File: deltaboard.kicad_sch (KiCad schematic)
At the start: 49 parts, among them J1 USB_C_Receptacle, J4 SM03B-SRSS-TB, SW1 SW_Push, SW2 SW_Push, U1 RP2350_80QFN, U2 NCP1117-3.3_SOT223, U3 W25Q128JVS, U4 DNF, Y1 ABM8-272-T3

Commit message: sajdashdjasdh
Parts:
- removed SW2: SW_Push, Button_Switch_SMD:SW_Push_1P1T_NO_Vertical_Wuerth_434133025816, symbol Switch:SW_Push
- added D1: D, symbol Device:D
- added JP1, JP2: Jumper_2_Open, symbol Jumper:Jumper_2_Open
- SW1: footprint Button_Switch_SMD:SW_Push_1P1T_NO_Vertical_Wuerth_434133025816 -> (none)
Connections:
- net GND: now also JP1.1 (A); no longer SW1.1
- net RUN: now also JP2.2 (B)
- net ~{USB_BOOT}: now also JP1.2 (B); no longer SW1.2
- net at R4.1: now also JP2.1 (A)
- new net: D1.2 (A), SW1.2
- new net COL0: SW1.1
- new net ROW0: D1.1 (K)
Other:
- note added: "BOOTSEL"
- note added: "RUN"

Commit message: add switches
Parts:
- removed SW1: SW_Push, symbol Switch:SW_Push
- added D10, D11, D12, D13, D14, D15, D16, D17, D18, D19, D2, D20, D21, D22, D23, D24, D25, D26, D27, D28, D29, D3, D30, D31, D32, D33, D34, D35, D36, D37, D38, D39, D4, D40, D41, D42, D43, D44, D45, D46, D47, D48, D49, D5, D50, D51, D52, D53, D54, D55, D56, D57, D58, D59, D6, D60, D61, D62, D63, D64, D65, D66, D67, D68, D69, D7, D70, D71, D72, D73, D74, D75, D76, D77, D78, D79, D8, D80, D81, D82, D83, D84, D9: D, Diode_SMD:D_0805_2012Metric_Pad1.15x1.40mm_HandSolder, symbol Device:D
- added K1: Esc, Button_Switch_Keyboard:SW_Cherry_MX_1.00u_PCB, symbol Switch:SW_Push
- added K10: F9, Button_Switch_Keyboard:SW_Cherry_MX_1.00u_PCB, symbol Switch:SW_Push
- added K11: F10, Button_Switch_Keyboard:SW_Cherry_MX_1.00u_PCB, symbol Switch:SW_Push
- added K12: F11, Button_Switch_Keyboard:SW_Cherry_MX_1.00u_PCB, symbol Switch:SW_Push
- added K13: ~~,`, Button_Switch_Keyboard:SW_Cherry_MX_1.00u_PCB, symbol Switch:SW_Push
- added K14: !,1, Button_Switch_Keyboard:SW_Cherry_MX_1.00u_PCB, symbol Switch:SW_Push
- added K15: @,2, Button_Switch_Keyboard:SW_Cherry_MX_1.00u_PCB, symbol Switch:SW_Push
- added K16: #,3, Button_Switch_Keyboard:SW_Cherry_MX_1.00u_PCB, symbol Switch:SW_Push
- added K17: $,4, Button_Switch_Keyboard:SW_Cherry_MX_1.00u_PCB, symbol Switch:SW_Push
- added K18: %,5, Button_Switch_Keyboard:SW_Cherry_MX_1.00u_PCB, symbol Switch:SW_Push
- added K19: ^,6, Button_Switch_Keyboard:SW_Cherry_MX_1.00u_PCB, symbol Switch:SW_Push
- added K2: F1, Button_Switch_Keyboard:SW_Cherry_MX_1.00u_PCB, symbol Switch:SW_Push
- added K20: &,7, Button_Switch_Keyboard:SW_Cherry_MX_1.00u_PCB, symbol Switch:SW_Push
- added K21: *,8, Button_Switch_Keyboard:SW_Cherry_MX_1.00u_PCB, symbol Switch:SW_Push
- added K22: (,9, Button_Switch_Keyboard:SW_Cherry_MX_1.00u_PCB, symbol Switch:SW_Push
- added K23: ),0, Button_Switch_Keyboard:SW_Cherry_MX_1.00u_PCB, symbol Switch:SW_Push
- added K24: _,-, Button_Switch_Keyboard:SW_Cherry_MX_1.00u_PCB, symbol Switch:SW_Push
- added K25: +,=, Button_Switch_Keyboard:SW_Cherry_MX_1.00u_PCB, symbol Switch:SW_Push
- added K26: Backspace, Button_Switch_Keyboard:SW_Cherry_MX_2.00u_PCB, symbol Switch:SW_Push
- added K27: F12, Button_Switch_Keyboard:SW_Cherry_MX_1.00u_PCB, symbol Switch:SW_Push
- added K28: Insert, Button_Switch_Keyboard:SW_Cherry_MX_1.00u_PCB, symbol Switch:SW_Push
- added K29: Home, Button_Switch_Keyboard:SW_Cherry_MX_1.00u_PCB, symbol Switch:SW_Push
- added K3: F2, Button_Switch_Keyboard:SW_Cherry_MX_1.00u_PCB, symbol Switch:SW_Push
- added K30: Tab, Button_Switch_Keyboard:SW_Cherry_MX_1.50u_PCB, symbol Switch:SW_Push
- added K31: Q, Button_Switch_Keyboard:SW_Cherry_MX_1.00u_PCB, symbol Switch:SW_Push
- added K32: W, Button_Switch_Keyboard:SW_Cherry_MX_1.00u_PCB, symbol Switch:SW_Push
- added K33: E, Button_Switch_Keyboard:SW_Cherry_MX_1.00u_PCB, symbol Switch:SW_Push
- added K34: R, Button_Switch_Keyboard:SW_Cherry_MX_1.00u_PCB, symbol Switch:SW_Push
- added K35: T, Button_Switch_Keyboard:SW_Cherry_MX_1.00u_PCB, symbol Switch:SW_Push
- added K36: Y, Button_Switch_Keyboard:SW_Cherry_MX_1.00u_PCB, symbol Switch:SW_Push
- added K37: U, Button_Switch_Keyboard:SW_Cherry_MX_1.00u_PCB, symbol Switch:SW_Push
- added K38: I, Button_Switch_Keyboard:SW_Cherry_MX_1.00u_PCB, symbol Switch:SW_Push
- added K39: O, Button_Switch_Keyboard:SW_Cherry_MX_1.00u_PCB, symbol Switch:SW_Push
- added K4: F3, Button_Switch_Keyboard:SW_Cherry_MX_1.00u_PCB, symbol Switch:SW_Push
- added K40: P, Button_Switch_Keyboard:SW_Cherry_MX_1.00u_PCB, symbol Switch:SW_Push
- added K41: {,[, Button_Switch_Keyboard:SW_Cherry_MX_1.00u_PCB, symbol Switch:SW_Push
- added K42: },], Button_Switch_Keyboard:SW_Cherry_MX_1.00u_PCB, symbol Switch:SW_Push
- added K43: |,\, Button_Switch_Keyboard:SW_Cherry_MX_1.50u_PCB, symbol Switch:SW_Push
- added K44: Delete, Button_Switch_Keyboard:SW_Cherry_MX_1.00u_PCB, symbol Switch:SW_Push
- added K45: End, Button_Switch_Keyboard:SW_Cherry_MX_1.00u_PCB, symbol Switch:SW_Push
- added K46: PgUp, Button_Switch_Keyboard:SW_Cherry_MX_1.00u_PCB, symbol Switch:SW_Push
- added K47: Caps Lock, Button_Switch_Keyboard:SW_Cherry_MX_1.75u_PCB, symbol Switch:SW_Push
- added K48: A, Button_Switch_Keyboard:SW_Cherry_MX_1.00u_PCB, symbol Switch:SW_Push
- added K49: S, Button_Switch_Keyboard:SW_Cherry_MX_1.00u_PCB, symbol Switch:SW_Push
- added K5: F4, Button_Switch_Keyboard:SW_Cherry_MX_1.00u_PCB, symbol Switch:SW_Push
- added K50: D, Button_Switch_Keyboard:SW_Cherry_MX_1.00u_PCB, symbol Switch:SW_Push
- added K51: F, Button_Switch_Keyboard:SW_Cherry_MX_1.00u_PCB, symbol Switch:SW_Push
- added K52: G, Button_Switch_Keyboard:SW_Cherry_MX_1.00u_PCB, symbol Switch:SW_Push
- added K53: H, Button_Switch_Keyboard:SW_Cherry_MX_1.00u_PCB, symbol Switch:SW_Push
- added K54: J, Button_Switch_Keyboard:SW_Cherry_MX_1.00u_PCB, symbol Switch:SW_Push
- added K55: K, Button_Switch_Keyboard:SW_Cherry_MX_1.00u_PCB, symbol Switch:SW_Push
- added K56: L, Button_Switch_Keyboard:SW_Cherry_MX_1.00u_PCB, symbol Switch:SW_Push
- added K57: :,;, Button_Switch_Keyboard:SW_Cherry_MX_1.00u_PCB, symbol Switch:SW_Push
- added K58: ",', Button_Switch_Keyboard:SW_Cherry_MX_1.00u_PCB, symbol Switch:SW_Push
- added K59: Enter, Button_Switch_Keyboard:SW_Cherry_MX_2.25u_PCB, symbol Switch:SW_Push
- added K6: F5, Button_Switch_Keyboard:SW_Cherry_MX_1.00u_PCB, symbol Switch:SW_Push
- added K60: Shift, Button_Switch_Keyboard:SW_Cherry_MX_2.25u_PCB, symbol Switch:SW_Push
- added K61: Z, Button_Switch_Keyboard:SW_Cherry_MX_1.00u_PCB, symbol Switch:SW_Push
- added K62: X, Button_Switch_Keyboard:SW_Cherry_MX_1.00u_PCB, symbol Switch:SW_Push
- added K63: C, Button_Switch_Keyboard:SW_Cherry_MX_1.00u_PCB, symbol Switch:SW_Push
- added K64: V, Button_Switch_Keyboard:SW_Cherry_MX_1.00u_PCB, symbol Switch:SW_Push
- added K65: B, Button_Switch_Keyboard:SW_Cherry_MX_1.00u_PCB, symbol Switch:SW_Push
- added K66: N, Button_Switch_Keyboard:SW_Cherry_MX_1.00u_PCB, symbol Switch:SW_Push
- added K67: M, Button_Switch_Keyboard:SW_Cherry_MX_1.00u_PCB, symbol Switch:SW_Push
- added K68: <,,, Button_Switch_Keyboard:SW_Cherry_MX_1.00u_PCB, symbol Switch:SW_Push
- added K69: >,., Button_Switch_Keyboard:SW_Cherry_MX_1.00u_PCB, symbol Switch:SW_Push
- added K7: F6, Button_Switch_Keyboard:SW_Cherry_MX_1.00u_PCB, symbol Switch:SW_Push
- added K70: ?,/, Button_Switch_Keyboard:SW_Cherry_MX_1.00u_PCB, symbol Switch:SW_Push
- added K71: Shift, Button_Switch_Keyboard:SW_Cherry_MX_2.75u_PCB, symbol Switch:SW_Push
- added K72: ↑, Button_Switch_Keyboard:SW_Cherry_MX_1.00u_PCB, symbol Switch:SW_Push
- added K73, K80: Ctrl, Button_Switch_Keyboard:SW_Cherry_MX_1.25u_PCB, symbol Switch:SW_Push
- added K74, K78: Win, Button_Switch_Keyboard:SW_Cherry_MX_1.25u_PCB, symbol Switch:SW_Push
- added K75, K77: Alt, Button_Switch_Keyboard:SW_Cherry_MX_1.25u_PCB, symbol Switch:SW_Push
- added K76: Blank, Button_Switch_Keyboard:SW_Cherry_MX_6.25u_PCB, symbol Switch:SW_Push
- added K79: Menu, Button_Switch_Keyboard:SW_Cherry_MX_1.25u_PCB, symbol Switch:SW_Push
- added K8: F7, Button_Switch_Keyboard:SW_Cherry_MX_1.00u_PCB, symbol Switch:SW_Push
- added K81: ←, Button_Switch_Keyboard:SW_Cherry_MX_1.00u_PCB, symbol Switch:SW_Push
- added K82: ↓, Button_Switch_Keyboard:SW_Cherry_MX_1.00u_PCB, symbol Switch:SW_Push
- added K83: PgDn, Button_Switch_Keyboard:SW_Cherry_MX_1.00u_PCB, symbol Switch:SW_Push
- added K84: →, Button_Switch_Keyboard:SW_Cherry_MX_1.00u_PCB, symbol Switch:SW_Push
- added K9: F8, Button_Switch_Keyboard:SW_Cherry_MX_1.00u_PCB, symbol Switch:SW_Push
- D1: footprint (none) -> Diode_SMD:D_0805_2012Metric_Pad1.15x1.40mm_HandSolder
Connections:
- net at D1.2 (A): now also K1.2
- net ROW0 renamed Row_0
- net Row_0: now also D10.1 (K), D11.1 (K), D12.1 (K), D2.1 (K), D27.1 (K), D3.1 (K), D4.1 (K), D5.1 (K), D6.1 (K), D7.1 (K), D8.1 (K), D9.1 (K)
- new net: D80.2 (A), K80.2
- new net: D49.2 (A), K49.2
- new net: D15.2 (A), K15.2
- new net: D6.2 (A), K6.2
- new net: D16.2 (A), K16.2
- new net: D41.2 (A), K41.2
- new net: D19.2 (A), K19.2
- new net: D36.2 (A), K36.2
- new net: D51.2 (A), K51.2
- new net: D47.2 (A), K47.2
- new net: D31.2 (A), K31.2
- new net: D61.2 (A), K61.2
- new net: D17.2 (A), K17.2
- new net: D13.2 (A), K13.2
- new net: D38.2 (A), K38.2
- new net: D53.2 (A), K53.2
- new net: D11.2 (A), K11.2
- new net: D12.2 (A), K12.2
- new net: D48.2 (A), K48.2
- new net: D52.2 (A), K52.2
- new net: D62.2 (A), K62.2
- new net: D66.2 (A), K66.2
- new net: D56.2 (A), K56.2
- new net: D34.2 (A), K34.2
- new net: D24.2 (A), K24.2
- new net: D35.2 (A), K35.2
- new net: D65.2 (A), K65.2
- new net: D8.2 (A), K8.2
- new net: D2.2 (A), K2.2
- new net: D55.2 (A), K55.2
- new net: D40.2 (A), K40.2
- new net: D75.2 (A), K75.2
- new net: D67.2 (A), K67.2
- new net: D25.2 (A), K25.2
- new net: D69.2 (A), K69.2
- new net: D79.2 (A), K79.2
- new net: D76.2 (A), K76.2
- new net: D23.2 (A), K23.2
- new net: D64.2 (A), K64.2
- new net: D39.2 (A), K39.2
- new net: D44.2 (A), K44.2
- new net: D30.2 (A), K30.2
- new net: D83.2 (A), K83.2
- new net: D10.2 (A), K10.2
- new net: D82.2 (A), K82.2
- new net: D7.2 (A), K7.2
- new net: D28.2 (A), K28.2
- new net: D20.2 (A), K20.2
- new net: D77.2 (A), K77.2
- new net: D46.2 (A), K46.2
- new net: D74.2 (A), K74.2
- new net: D14.2 (A), K14.2
- new net: D45.2 (A), K45.2
- new net: D29.2 (A), K29.2
- new net: D70.2 (A), K70.2
- new net: D9.2 (A), K9.2
- new net: D37.2 (A), K37.2
- new net: D63.2 (A), K63.2
- new net: D81.2 (A), K81.2
- new net: D5.2 (A), K5.2
- new net: D84.2 (A), K84.2
- new net: D50.2 (A), K50.2
- new net: D32.2 (A), K32.2
- new net: D60.2 (A), K60.2
- new net: D71.2 (A), K71.2
- new net: D33.2 (A), K33.2
- new net: D57.2 (A), K57.2
- new net: D4.2 (A), K4.2
- new net: D21.2 (A), K21.2
- new net: D27.2 (A), K27.2
- new net: D42.2 (A), K42.2
- new net: D78.2 (A), K78.2
- new net: D68.2 (A), K68.2
- new net: D54.2 (A), K54.2
- new net: D18.2 (A), K18.2
- new net: D22.2 (A), K22.2
- new net: D59.2 (A), K59.2
- new net: D72.2 (A), K72.2
- new net: D58.2 (A), K58.2
- new net: D73.2 (A), K73.2
- new net: D3.2 (A), K3.2
- new net: D43.2 (A), K43.2
- new net: D26.2 (A), K26.2
- new net Col_0: K1.1, K13.1, K30.1, K47.1, K60.1, K73.1
- new net Col_1: K14.1, K2.1, K31.1, K48.1, K61.1, K74.1
- new net Col_10: K11.1, K23.1, K40.1, K57.1, K70.1, K84.1
- new net Col_11: K12.1, K24.1, K41.1, K58.1, K71.1
- new net Col_12: K25.1, K27.1, K42.1, K59.1, K72.1
- new net Col_13: K26.1, K43.1
- new net Col_14: K28.1, K44.1
- new net Col_15: K29.1, K45.1
- new net Col_16: K46.1, K83.1
- new net Col_2: K15.1, K3.1, K32.1, K49.1, K62.1, K75.1
- new net Col_3: K16.1, K33.1, K4.1, K50.1, K63.1, K76.1
- new net Col_4: K17.1, K34.1, K5.1, K51.1, K64.1, K77.1
- new net Col_5: K18.1, K35.1, K52.1, K6.1, K65.1, K78.1
- new net Col_6: K19.1, K36.1, K53.1, K66.1, K7.1, K79.1
- new net Col_7: K20.1, K37.1, K54.1, K67.1, K8.1, K80.1
- new net Col_8: K21.1, K38.1, K55.1, K68.1, K81.1, K9.1
- new net Col_9: K10.1, K22.1, K39.1, K56.1, K69.1, K82.1
- new net Row_1: D13.1 (K), D14.1 (K), D15.1 (K), D16.1 (K), D17.1 (K), D18.1 (K), D19.1 (K), D20.1 (K), D21.1 (K), D22.1 (K), D23.1 (K), D24.1 (K), D25.1 (K), D26.1 (K), D28.1 (K), D29.1 (K), D46.1 (K)
- new net Row_2: D30.1 (K), D31.1 (K), D32.1 (K), D33.1 (K), D34.1 (K), D35.1 (K), D36.1 (K), D37.1 (K), D38.1 (K), D39.1 (K), D40.1 (K), D41.1 (K), D42.1 (K), D43.1 (K), D44.1 (K), D45.1 (K), D83.1 (K)
- new net Row_3: D47.1 (K), D48.1 (K), D49.1 (K), D50.1 (K), D51.1 (K), D52.1 (K), D53.1 (K), D54.1 (K), D55.1 (K), D56.1 (K), D57.1 (K), D58.1 (K), D59.1 (K)
- new net Row_4: D60.1 (K), D61.1 (K), D62.1 (K), D63.1 (K), D64.1 (K), D65.1 (K), D66.1 (K), D67.1 (K), D68.1 (K), D69.1 (K), D70.1 (K), D71.1 (K), D72.1 (K)
- new net Row_5: D73.1 (K), D74.1 (K), D75.1 (K), D76.1 (K), D77.1 (K), D78.1 (K), D79.1 (K), D80.1 (K), D81.1 (K), D82.1 (K), D84.1 (K)
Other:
- moved on the sheet: C6, C7, JP2, R4

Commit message: rename some labels
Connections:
- net Col_0 renamed COL_0
- net Col_1 renamed COL_1
- net Col_10 renamed COL_10
- net Col_11 renamed COL_11
- net Col_12 renamed COL_12
- net Col_13 renamed COL_13
- net Col_14 renamed COL_14
- net Col_15 renamed COL_15
- net Col_16 renamed COL_16
- net Col_2 renamed COL_2
- net Col_3 renamed COL_3
- net Col_4 renamed COL_4
- net Col_5 renamed COL_5
- net Col_6 renamed COL_6
- net Col_7 renamed COL_7
- net Col_8 renamed COL_8
- net Col_9 renamed COL_9
- net Row_0 renamed ROW_0
- net Row_1 renamed ROW_1
- net Row_2 renamed ROW_2
- net Row_3 renamed ROW_3
- net Row_4 renamed ROW_4
- net Row_5 renamed ROW_5
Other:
- moved on the sheet: D1, D10, D11, D12, D13, D14, D15, D16, D17, D18, D19, D2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

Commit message: feat: add switches and leds
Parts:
- removed C11, C12, C13: 100n, Capacitor_SMD:C_0402_1005Metric, symbol Device:C
- removed C4: 15p, Capacitor_SMD:C_0402_1005Metric, symbol Device:C
- removed C9: 4.7u, Capacitor_SMD:C_0402_1005Metric, symbol Device:C
- removed J4: SM03B-SRSS-TB, Connector_JST:JST_SH_SM03B-SRSS-TB_1x03-1MP_P1.00mm_Horizontal, symbol Connector_Generic_MountingPin:Conn_01x03_MountingPin
- removed K32: W, Button_Switch_Keyboard:SW_Cherry_MX_1.00u_PCB, symbol Switch:SW_Push
- removed L1: 3.3u, RP2350_80QFN_minimal:L_pol_2016, symbol Device:L
- removed R10: 0, Resistor_SMD:R_0402_1005Metric, symbol Device:R
- removed R11, R13: DNF, Resistor_SMD:R_0402_1005Metric, symbol Device:R
- removed R12: 5.1k, symbol Device:R
- removed R2, R4: 1k, Resistor_SMD:R_0402_1005Metric, symbol Device:R
- removed R3: 33, Resistor_SMD:R_0402_1005Metric, symbol Device:R
- removed U1: RP2350_80QFN, RP2350_80QFN_minimal:RP2350-QFN-80-1EP_10x10_P0.4mm_EP3.4x3.4mm_ThermalVias, symbol MCU_RaspberryPi_RP2350:RP2350_80QFN
- removed U4: DNF, Package_SO:SOIC-8_5.23x5.23mm_P1.27mm, symbol Memory_Flash:W25Q128JVS
- added C16: 100n, Capacitor_SMD:C_0402_1005Metric, symbol Device:C
- added C18, C19, C20, C23, C24, C25: 2.2uF, symbol Device:C
- added C2: 15p, Capacitor_SMD:C_0402_1005Metric, symbol Device:C
- added D85, D86, D87: D, Diode_SMD:D_0805_2012Metric_Pad1.15x1.40mm_HandSolder, symbol Device:D
- added H5, H6, H7, H8: MountingHole, MountingHole:MountingHole_2.7mm_M2.5, symbol Mechanical:MountingHole
- added J2: Conn_01x04, symbol Connector_Generic:Conn_01x04
- added K85: ↓, Button_Switch_Keyboard:SW_Cherry_MX_1.00u_PCB, symbol Switch:SW_Push
- added K86: PgDn, Button_Switch_Keyboard:SW_Cherry_MX_1.00u_PCB, symbol Switch:SW_Push
- added K87: →, Button_Switch_Keyboard:SW_Cherry_MX_1.00u_PCB, symbol Switch:SW_Push
- added LED1, LED10, LED11, LED12, LED13, LED14, LED15, LED16, LED17, LED18, LED19, LED2, LED20, LED21, LED22, LED23, LED24, LED25, LED26, LED27, LED28, LED29, LED3, LED30, LED31, LED32, LED33, LED34, LED35, LED36, LED37, LED38, LED39, LED4, LED40, LED41, LED42, LED43, LED44, LED45, LED46, LED47, LED48, LED49, LED5, LED50, LED51, LED52, LED53, LED54, LED55, LED56, LED57, LED58, LED59, LED6, LED60, LED61, LED62, LED63, LED64, LED65, LED66, LED67, LED68, LED69, LED7, LED70, LED71, LED72, LED73, LED74, LED75, LED76, LED77, LED78, LED79, LED8, LED80, LED81, LED82, LED83, LED84, LED85, LED86, LED9: SK6812MINI-E, neopixel.petty:SK6812MINI-E, symbol neopixel:SK6812MINI
- added R1: 1k, Resistor_SMD:R_0402_1005Metric, symbol Device:R
- added R8: 5.1k, symbol Device:R
- added SW1: SW_SPST, symbol Switch:SW_SPST
- added SW11: RotaryEncoder_Switch, Components:encoder, symbol Device:RotaryEncoder_Switch
- added U3: RP2040, RP2040_minimal:RP2040-QFN-56, symbol MCU_RaspberryPi_RP2040:RP2040
- C10: value 4.7u -> 1u
- C21: value 100n -> 2.2uF; footprint Capacitor_SMD:C_0402_1005Metric -> (none)
- C22: value DNF -> 2.2uF; footprint Capacitor_SMD:C_0402_1005Metric -> (none)
- C6, C7: value 4.7u -> 100n; footprint RP2350_80QFN_minimal:C_0402_1005Metric_small_pads -> Capacitor_SMD:C_0402_1005Metric
- C8: value 100n -> 1u
- K13: value ~~,` -> F12
- K14: value !,1 -> Blank
- K15: value @,2 -> Blank
- K16: value #,3 -> ~~,`
- K17: value $,4 -> !,1
- K18: value %,5 -> @,2
- K19: value ^,6 -> #,3
- K20: value &,7 -> $,4
- K21: value *,8 -> %,5
- K22: value (,9 -> ^,6
- K23: value ),0 -> &,7
- K24: value _,- -> *,8
- K25: value +,= -> (,9
- K26: value Backspace -> ),0; footprint Button_Switch_Keyboard:SW_Cherry_MX_2.00u_PCB -> Button_Switch_Keyboard:SW_Cherry_MX_1.00u_PCB
- K27: value F12 -> _,-
- K28: value Insert -> +,=
- K29: value Home -> Backspace; footprint Button_Switch_Keyboard:SW_Cherry_MX_1.00u_PCB -> Button_Switch_Keyboard:SW_Cherry_MX_2.00u_PCB
- K30: value Tab -> Insert; footprint Button_Switch_Keyboard:SW_Cherry_MX_1.50u_PCB -> Button_Switch_Keyboard:SW_Cherry_MX_1.00u_PCB
- K31: value Q -> Home
- K33: value E -> Tab; footprint Button_Switch_Keyboard:SW_Cherry_MX_1.00u_PCB -> Button_Switch_Keyboard:SW_Cherry_MX_1.50u_PCB
- K34: value R -> Q
- K35: value T -> W
- K36: value Y -> E
- K37: value U -> R
- K38: value I -> T
- K39: value O -> Y
- K40: value P -> U
- K41: value {,[ -> I
- K42: value },] -> O
- K43: value |,\ -> P; footprint Button_Switch_Keyboard:SW_Cherry_MX_1.50u_PCB -> Button_Switch_Keyboard:SW_Cherry_MX_1.00u_PCB
- K44: value Delete -> {,[
- K45: value End -> },]
- K46: value PgUp -> |,\; footprint Button_Switch_Keyboard:SW_Cherry_MX_1.00u_PCB -> Button_Switch_Keyboard:SW_Cherry_MX_1.50u_PCB
- K47: value Caps Lock -> Delete; footprint Button_Switch_Keyboard:SW_Cherry_MX_1.75u_PCB -> Button_Switch_Keyboard:SW_Cherry_MX_1.00u_PCB
- K48: value A -> End
- K49: value S -> PgUp
- K50: value D -> Caps Lock; footprint Button_Switch_Keyboard:SW_Cherry_MX_1.00u_PCB -> Button_Switch_Keyboard:SW_Cherry_MX_1.75u_PCB
- K51: value F -> A
- K52: value G -> S
- K53: value H -> D
- K54: value J -> F
- K55: value K -> G
- K56: value L -> H
- K57: value :,; -> J
- K58: value ",' -> K
- K59: value Enter -> L; footprint Button_Switch_Keyboard:SW_Cherry_MX_2.25u_PCB -> Button_Switch_Keyboard:SW_Cherry_MX_1.00u_PCB
- K60: value Shift -> :,;; footprint Button_Switch_Keyboard:SW_Cherry_MX_2.25u_PCB -> Button_Switch_Keyboard:SW_Cherry_MX_1.00u_PCB
- K61: value Z -> ",'
- K62: value X -> Enter; footprint Button_Switch_Keyboard:SW_Cherry_MX_1.00u_PCB -> Button_Switch_Keyboard:SW_Cherry_MX_2.25u_PCB
- K63: value C -> Shift; footprint Button_Switch_Keyboard:SW_Cherry_MX_1.00u_PCB -> Button_Switch_Keyboard:SW_Cherry_MX_2.25u_PCB
- K64: value V -> Z
- K65: value B -> X
- K66: value N -> C
- K67: value M -> V
- K68: value <,, -> B
- K69: value >,. -> N
- K70: value ?,/ -> M
- K71: value Shift -> <,,; footprint Button_Switch_Keyboard:SW_Cherry_MX_2.75u_PCB -> Button_Switch_Keyboard:SW_Cherry_MX_1.00u_PCB
- K72: value ↑ -> >,.
- K73: value Ctrl -> ?,/; footprint Button_Switch_Keyboard:SW_Cherry_MX_1.25u_PCB -> Button_Switch_Keyboard:SW_Cherry_MX_1.00u_PCB
- K74: value Win -> Shift; footprint Button_Switch_Keyboard:SW_Cherry_MX_1.25u_PCB -> Button_Switch_Keyboard:SW_Cherry_MX_2.75u_PCB
- K75: value Alt -> ↑; footprint Button_Switch_Keyboard:SW_Cherry_MX_1.25u_PCB -> Button_Switch_Keyboard:SW_Cherry_MX_1.00u_PCB
- K76: value Blank -> Ctrl; footprint Button_Switch_Keyboard:SW_Cherry_MX_6.25u_PCB -> Button_Switch_Keyboard:SW_Cherry_MX_1.25u_PCB
- K77: value Alt -> Win
- K78: value Win -> Alt
- K79: value Menu -> Blank; footprint Button_Switch_Keyboard:SW_Cherry_MX_1.25u_PCB -> Button_Switch_Keyboard:SW_Cherry_MX_6.25u_PCB
- K80: value Ctrl -> Alt
- K81: value ← -> Win; footprint Button_Switch_Keyboard:SW_Cherry_MX_1.00u_PCB -> Button_Switch_Keyboard:SW_Cherry_MX_1.25u_PCB
- K82: value ↓ -> Menu; footprint Button_Switch_Keyboard:SW_Cherry_MX_1.00u_PCB -> Button_Switch_Keyboard:SW_Cherry_MX_1.25u_PCB
- K83: value PgDn -> Ctrl; footprint Button_Switch_Keyboard:SW_Cherry_MX_1.00u_PCB -> Button_Switch_Keyboard:SW_Cherry_MX_1.25u_PCB
- K84: value → -> ←
- R5: value 5.1k -> 1k; footprint (none) -> Resistor_SMD:R_0402_1005Metric
- R6: footprint Resistor_SMD:R_0402_1005Metric -> (none)
- R9: value DNF -> 5.1k; footprint Resistor_SMD:R_0402_1005Metric -> (none)
- renumbered C15 to C11, C16 to C12, C17 to C13, C18 to C14, C20 to C15, C19 to C17, C5 to C4, C2 to C5, C14 to C9, R1 to R2, R7 to R3, R8 to R4, U2 to U1, U3 to U2
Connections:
- net +1V1: now also C6.1, U3.23 (DVDD), U3.45 (VREG_VOUT), U3.50 (DVDD); no longer C10.1
- net +3V3: now also C10.1, C16.1, U3.1 (IOVDD), U3.10 (IOVDD), U3.22 (IOVDD), U3.33 (IOVDD), U3.42 (IOVDD), U3.43 (ADC_AVDD), U3.44 (VREG_IN), U3.48 (USB_VDD), U3.49 (IOVDD); no longer C21.1, C22.1, C6.1
- net COL_0: now also K16.1, K33.1, K50.1, K63.1, K76.1, U3.8 (GPIO6); no longer K13.1, K30.1, K47.1, K60.1, K73.1
- net COL_1: now also K17.1, K34.1, K51.1, K64.1, K77.1, U3.9 (GPIO7); no longer K14.1, K31.1, K48.1, K61.1, K74.1
- net COL_10: now also K26.1, K43.1, K60.1, K73.1, K87.1, U3.27 (GPIO16); no longer K23.1, K40.1, K57.1, K70.1, K84.1
- net COL_11: now also K27.1, K44.1, K61.1, K74.1, U3.28 (GPIO17); no longer K24.1, K41.1, K58.1, K71.1
- net COL_12: now also K13.1, K28.1, K45.1, K62.1, K75.1, U3.29 (GPIO18); no longer K25.1, K27.1, K42.1, K59.1, K72.1
- net COL_13: now also K14.1, K29.1, K46.1, U3.30 (GPIO19); no longer K26.1, K43.1
- net COL_14: now also K15.1, K30.1, K47.1, U3.31 (GPIO20); no longer K28.1, K44.1
- net COL_16: now also K49.1, K86.1, U3.34 (GPIO22); no longer K46.1, K83.1
- net COL_2: now also K18.1, K35.1, K52.1, K65.1, K78.1, U3.11 (GPIO8); no longer K15.1, K49.1, K62.1, K75.1
- net COL_3: now also K19.1, K36.1, K53.1, K66.1, K79.1, U3.12 (GPIO9); no longer K16.1, K33.1, K50.1, K63.1, K76.1
- net COL_4: now also K20.1, K37.1, K54.1, K67.1, K80.1, U3.13 (GPIO10); no longer K17.1, K34.1, K51.1, K64.1, K77.1
- net COL_5: now also K21.1, K38.1, K55.1, K68.1, K81.1, U3.14 (GPIO11); no longer K18.1, K35.1, K52.1, K65.1, K78.1
- net COL_6: now also K22.1, K39.1, K56.1, K69.1, K82.1, U3.15 (GPIO12); no longer K19.1, K36.1, K53.1, K66.1, K79.1
- net COL_7: now also K23.1, K40.1, K57.1, K70.1, K83.1, U3.16 (GPIO13); no longer K20.1, K37.1, K54.1, K67.1, K80.1
- net COL_8: now also K24.1, K41.1, K58.1, K71.1, K84.1, U3.17 (GPIO14); no longer K21.1, K38.1, K55.1, K68.1, K81.1
- net COL_9: now also K25.1, K42.1, K59.1, K72.1, K85.1, U3.18 (GPIO15); no longer K22.1, K39.1, K56.1, K69.1, K82.1
- net GND: now also JP2.1 (A), R9.2, C16.2, C18.2, C19.2, C2.2, C20.2, C23.2, C24.2, C25.2, J2.1 (Pin_1), LED1.2 (VSS), LED10.2 (VSS), LED11.2 (VSS), LED12.2 (VSS), LED13.2 (VSS), LED14.2 (VSS), LED15.2 (VSS), LED16.2 (VSS), LED17.2 (VSS), LED18.2 (VSS), LED19.2 (VSS), LED2.2 (VSS), LED20.2 (VSS), LED21.2 (VSS), LED22.2 (VSS), LED23.2 (VSS), LED24.2 (VSS), LED25.2 (VSS), LED26.2 (VSS), LED27.2 (VSS), LED28.2 (VSS), LED29.2 (VSS), LED3.2 (VSS), LED30.2 (VSS), LED31.2 (VSS), LED32.2 (VSS), LED33.2 (VSS), LED34.2 (VSS), LED35.2 (VSS)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; no longer R5.2
- net GPIO0: now also D1.1 (K), D10.1 (K), D11.1 (K), D12.1 (K), D13.1 (K), D14.1 (K), D15.1 (K), D2.1 (K), D3.1 (K), D32.1 (K), D4.1 (K), D5.1 (K), D6.1 (K), D7.1 (K), D8.1 (K), D9.1 (K), U3.2 (GPIO0); no longer R9.1
- net GPIO1: now also D16.1 (K), D17.1 (K), D18.1 (K), D19.1 (K), D20.1 (K), D21.1 (K), D22.1 (K), D23.1 (K), D24.1 (K), D25.1 (K), D26.1 (K), D27.1 (K), D28.1 (K), D29.1 (K), D30.1 (K), D31.1 (K), D49.1 (K), U3.3 (GPIO1)
- net GPIO2: now also D33.1 (K), D34.1 (K), D35.1 (K), D36.1 (K), D37.1 (K), D38.1 (K), D39.1 (K), D40.1 (K), D41.1 (K), D42.1 (K), D43.1 (K), D44.1 (K), D45.1 (K), D46.1 (K), D47.1 (K), D48.1 (K), D86.1 (K), U3.4 (GPIO2)
- net GPIO3: now also D50.1 (K), D51.1 (K), D52.1 (K), D53.1 (K), D54.1 (K), D55.1 (K), D56.1 (K), D57.1 (K), D58.1 (K), D59.1 (K), D60.1 (K), D61.1 (K), D62.1 (K), U3.5 (GPIO3)
- net GPIO4: now also D63.1 (K), D64.1 (K), D65.1 (K), D66.1 (K), D67.1 (K), D68.1 (K), D69.1 (K), D70.1 (K), D71.1 (K), D72.1 (K), D73.1 (K), D74.1 (K), D75.1 (K), U3.6 (GPIO4)
- net GPIO5: now also D76.1 (K), D77.1 (K), D78.1 (K), D79.1 (K), D80.1 (K), D81.1 (K), D82.1 (K), D83.1 (K), D84.1 (K), D85.1 (K), D87.1 (K), U3.7 (GPIO5)
- net QSPI_SCLK: now also U3.52 (QSPI_SCLK)
- net QSPI_SD0: now also U3.53 (QSPI_SD0)
- net QSPI_SD1: now also U3.55 (QSPI_SD1)
- net QSPI_SD2: now also U3.54 (QSPI_SD2)
- net QSPI_SD3: now also U3.51 (QSPI_SD3)
- net QSPI_SS: now also R2.2, U2.1 (~{CS}), R1.1, U3.56 (QSPI_SS); no longer R6.1
- net RUN: now also R6.2, U3.26 (RUN); no longer JP2.2 (B)
- net SWCLK: now also U3.24 (SWCLK)
- net SWD: now also U3.25 (SWD)
- net VBUS: now also SW1.2 (B); no longer J1.A4 (VBUS), J1.A9 (VBUS), J1.B4 (VBUS), J1.B9 (VBUS)
- net XIN: now also C2.1, U3.20 (XIN); no longer C3.1
- net XOUT: now also R5.1, U3.21 (XOUT)
- net ~{USB_BOOT}: now also R1.2; no longer R6.2
- net at Y1.3: now also C3.1, R5.2
- net at R3.2: now also U3.47 (USB_DP)
- net at R4.2: now also U3.46 (USB_DM)
- net at J1.B5 (CC2): now also R9.1
- net at J1.A5 (CC1): now also R8.1; no longer R5.1
- net ENC_SWA: now reaches D32.2 (A)
- net ENC_SWA: now also SW11.S2
- removed net COL_15: K29.1, K45.1
- removed net FLASH_SS: R2.2, R9.2, U2.1 (~{CS})
- removed net ROW_0: D1.1 (K), D10.1 (K), D11.1 (K), D12.1 (K), D2.1 (K), D27.1 (K), D3.1 (K), D4.1 (K), D5.1 (K), D6.1 (K), D7.1 (K), D8.1 (K), D9.1 (K)
- removed net ROW_1: D13.1 (K), D14.1 (K), D15.1 (K), D16.1 (K), D17.1 (K), D18.1 (K), D19.1 (K), D20.1 (K), D21.1 (K), D22.1 (K), D23.1 (K), D24.1 (K), D25.1 (K), D26.1 (K), D28.1 (K), D29.1 (K), D46.1 (K)
- removed net ROW_2: D30.1 (K), D31.1 (K), D32.1 (K), D33.1 (K), D34.1 (K), D35.1 (K), D36.1 (K), D37.1 (K), D38.1 (K), D39.1 (K), D40.1 (K), D41.1 (K), D42.1 (K), D43.1 (K), D44.1 (K), D45.1 (K), D83.1 (K)
- removed net ROW_3: D47.1 (K), D48.1 (K), D49.1 (K), D50.1 (K), D51.1 (K), D52.1 (K), D53.1 (K), D54.1 (K), D55.1 (K), D56.1 (K), D57.1 (K), D58.1 (K), D59.1 (K)
- removed net ROW_4: D60.1 (K), D61.1 (K), D62.1 (K), D63.1 (K), D64.1 (K), D65.1 (K), D66.1 (K), D67.1 (K), D68.1 (K), D69.1 (K), D70.1 (K), D71.1 (K), D72.1 (K)
- removed net ROW_5: D73.1 (K), D74.1 (K), D75.1 (K), D76.1 (K), D77.1 (K), D78.1 (K), D79.1 (K), D80.1 (K), D81.1 (K), D82.1 (K), D84.1 (K)
- new net: D86.2 (A), K86.2
- new net: LED61.1 (DOUT), LED62.3 (DIN)
- new net: LED60.1 (DOUT), LED61.3 (DIN)
- new net: JP2.2 (B), R6.1
- new net: LED26.1 (DOUT), LED27.3 (DIN)
- new net: LED25.1 (DOUT), LED26.3 (DIN)
- new net: LED28.1 (DOUT), LED29.3 (DIN)
- new net: LED27.1 (DOUT), LED28.3 (DIN)
- new net: LED65.1 (DOUT), LED66.3 (DIN)
- new net: LED64.1 (DOUT), LED65.3 (DIN)
- new net: LED13.1 (DOUT), LED14.3 (DIN)
- new net: LED12.1 (DOUT), LED13.3 (DIN)
- new net: LED68.1 (DOUT), LED69.3 (DIN)
- new net: LED67.1 (DOUT), LED68.3 (DIN)
- new net: LED24.1 (DOUT), LED25.3 (DIN)
- new net: LED48.1 (DOUT), LED49.3 (DIN)
- new net: LED47.1 (DOUT), LED48.3 (DIN)
- new net: LED78.1 (DOUT), LED79.3 (DIN)
- new net: LED77.1 (DOUT), LED78.3 (DIN)
- new net: LED58.1 (DOUT), LED59.3 (DIN)
- new net: LED57.1 (DOUT), LED58.3 (DIN)
- new net: LED29.1 (DOUT), LED30.3 (DIN)
- new net: LED10.1 (DOUT), LED11.3 (DIN)
- new net: LED10.3 (DIN), LED9.1 (DOUT)
- new net: LED59.1 (DOUT), LED60.3 (DIN)
- new net: LED8.1 (DOUT), LED9.3 (DIN)
- new net: LED6.1 (DOUT), LED7.3 (DIN)
- new net: LED5.1 (DOUT), LED6.3 (DIN)
- new net: D87.2 (A), K87.2
- new net: LED83.1 (DOUT), LED84.3 (DIN)
- new net: LED82.1 (DOUT), LED83.3 (DIN)
- new net: LED79.1 (DOUT), LED80.3 (DIN)
- new net: LED31.1 (DOUT), LED32.3 (DIN)
- new net: LED30.1 (DOUT), LED31.3 (DIN)
- new net: LED7.1 (DOUT), LED8.3 (DIN)
- new net: LED38.1 (DOUT), LED39.3 (DIN)
- new net: LED37.1 (DOUT), LED38.3 (DIN)
- new net: LED72.1 (DOUT), LED73.3 (DIN)
- new net: LED71.1 (DOUT), LED72.3 (DIN)
- new net: LED81.1 (DOUT), LED82.3 (DIN)
- new net: LED20.1 (DOUT), LED21.3 (DIN)
- new net: LED19.1 (DOUT), LED20.3 (DIN)
- new net: LED18.1 (DOUT), LED19.3 (DIN)
- new net: LED17.1 (DOUT), LED18.3 (DIN)
- new net: LED56.1 (DOUT), LED57.3 (DIN)
- new net: LED55.1 (DOUT), LED56.3 (DIN)
- new net: LED85.1 (DOUT), LED86.3 (DIN)
- new net: LED53.1 (DOUT), LED54.3 (DIN)
- new net: LED52.1 (DOUT), LED53.3 (DIN)
- new net: LED51.1 (DOUT), LED52.3 (DIN)
- new net: LED50.1 (DOUT), LED51.3 (DIN)
- new net: LED16.1 (DOUT), LED17.3 (DIN)
- new net: D85.2 (A), K85.2
- new net: LED69.1 (DOUT), LED70.3 (DIN)
- new net: LED21.1 (DOUT), LED22.3 (DIN)
- new net: LED80.1 (DOUT), LED81.3 (DIN)
- new net: LED54.1 (DOUT), LED55.3 (DIN)
- new net: LED23.1 (DOUT), LED24.3 (DIN)
- new net: LED76.1 (DOUT), LED77.3 (DIN)
- new net: LED36.1 (DOUT), LED37.3 (DIN)
- new net: LED35.1 (DOUT), LED36.3 (DIN)
- new net: LED73.1 (DOUT), LED74.3 (DIN)
- new net: LED63.1 (DOUT), LED64.3 (DIN)
- new net: LED33.1 (DOUT), LED34.3 (DIN)
- new net: LED74.1 (DOUT), LED75.3 (DIN)
- new net: J1.A4 (VBUS), J1.A9 (VBUS), J1.B4 (VBUS), J1.B9 (VBUS), SW1.1 (A)
- new net: LED2.1 (DOUT), LED3.3 (DIN)
- new net: LED1.1 (DOUT), LED2.3 (DIN)
- new net: LED3.1 (DOUT), LED4.3 (DIN)
- new net: LED22.1 (DOUT), LED23.3 (DIN)
- new net: LED4.1 (DOUT), LED5.3 (DIN)
- new net: LED45.1 (DOUT), LED46.3 (DIN)
- new net: LED44.1 (DOUT), LED45.3 (DIN)
- new net: LED42.1 (DOUT), LED43.3 (DIN)
- new net: LED41.1 (DOUT), LED42.3 (DIN)
- new net: LED40.1 (DOUT), LED41.3 (DIN)
- new net: LED39.1 (DOUT), LED40.3 (DIN)
- new net: LED46.1 (DOUT), LED47.3 (DIN)
- new net: LED11.1 (DOUT), LED12.3 (DIN)
- new net: LED34.1 (DOUT), LED35.3 (DIN)
- new net: LED70.1 (DOUT), LED71.3 (DIN)
- new net: LED14.1 (DOUT), LED15.3 (DIN)
- new net: LED43.1 (DOUT), LED44.3 (DIN)
- new net: LED84.1 (DOUT), LED85.3 (DIN)
- new net: LED66.1 (DOUT), LED67.3 (DIN)
- new net ENC_1_A: SW11.A, U3.39 (GPIO27_ADC1)
- new net ENC_1_B: SW11.B, U3.38 (GPIO26_ADC0)
- new net ENC_SWB: K31.1, K48.1, SW11.S1, U3.32 (GPIO21)
- new net GPIO28_ADC2: U3.40 (GPIO28_ADC2)
- new net GPIO29_ADC3: U3.41 (GPIO29_ADC3)
- new net I2C_SCL: J2.3 (Pin_3), U3.37 (GPIO25)
- new net I2C_SDA: J2.4 (Pin_4), U3.36 (GPIO24)
- new net LED: LED1.3 (DIN), U3.35 (GPIO23)
- new net LED_OUT_0: LED15.1 (DOUT), LED16.3 (DIN)
- new net LED_OUT_1: LED32.1 (DOUT), LED33.3 (DIN)
- new net LED_OUT_2: LED49.1 (DOUT), LED50.3 (DIN)
- new net LED_OUT_3: LED62.1 (DOUT), LED63.3 (DIN)
- new net LED_OUT_4: LED75.1 (DOUT), LED76.3 (DIN)
- new net VCC: C18.1, C19.1, C20.1, C21.1, C22.1, C23.1, C24.1, C25.1, J2.2 (Pin_2), LED1.4 (VDD), LED10.4 (VDD), LED11.4 (VDD), LED12.4 (VDD), LED13.4 (VDD), LED14.4 (VDD), LED15.4 (VDD), LED16.4 (VDD), LED17.4 (VDD), LED18.4 (VDD), LED19.4 (VDD), LED2.4 (VDD), LED20.4 (VDD), LED21.4 (VDD), LED22.4 (VDD), LED23.4 (VDD), LED24.4 (VDD), LED25.4 (VDD), LED26.4 (VDD), LED27.4 (VDD), LED28.4 (VDD), LED29.4 (VDD), LED3.4 (VDD), LED30.4 (VDD), LED31.4 (VDD), LED32.4 (VDD), LED33.4 (VDD), LED34.4 (VDD), LED35.4 (VDD), LED36.4 (VDD), LED37.4 (VDD)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
- no-connect marks 0 -> 2
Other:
- note added: "Crystal"
- note added: "Flash"
- note added: "LEDs"
- note added: "MCU"
- note added: "Make sure C10 is close to pin 44 of RP2040"
- note added: "Make sure C8 is close to pin 45 of RP2040"
- note added: "Make sure R3 and R4 are close to RP2040"
- note added: "OLED"
- note added: "Pin Mappings"
- note added: "Switches"
- note removed: "12MHz Clock (Crystal)"
- note removed: "BOOTSEL"
- note removed: "JST Debug Connector"
- note removed: "Make sure R7 and R8 are close to RP2350"
- note removed: "Optional Secondary flash or PSRAM (U4), using the second chip select (XIP_SS_N[1]) on GPIO0. N.B. Pull-up R13 will be required as GPIOs default to pull-downs at power-up."
- note removed: "Primary Flash"
- note removed: "RUN"
- note removed: "Secondary Flash/PSRAM"
- moved on the sheet: C1, C11, C12, C13, C14, C15, C17, C4, C5, C9, H1, H2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

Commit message: update footprints
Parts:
- C18, C19, C20, C21, C22, C23, C24, C25: footprint (none) -> Capacitor_SMD:C_0603_1608Metric
- D1, D10, D11, D12, D13, D14, D15, D16, D17, D18, D19, D2, D20, D21, D22, D23, D24, D25, D26, D27, D28, D29, D3, D30, D31, D32, D33, D34, D35, D36, D37, D38, D39, D4, D40, D41, D42, D43, D44, D45, D46, D47, D48, D49, D5, D50, D51, D52, D53, D54, D55, D56, D57, D58, D59, D6, D60, D61, D62, D63, D64, D65, D66, D67, D68, D69, D7, D70, D71, D72, D73, D74, D75, D76, D77, D78, D79, D8, D80, D81, D82, D83, D84, D85, D86, D87, D9: footprint Diode_SMD:D_0805_2012Metric_Pad1.15x1.40mm_HandSolder -> Diode_SMD:D_SOD-123

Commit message: feat: place most leds
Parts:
- J1: footprint (none) -> Components:USB-C_SMD-TYPE-C-31-M-12
- J2: footprint (none) -> Components:SSD1306-0.91-OLED-4pin-128x32
- JP1, JP2: footprint (none) -> Jumper:SolderJumper-2_P1.3mm_Open_TrianglePad1.0x1.5mm
- R6, R8, R9: footprint (none) -> Resistor_SMD:R_0402_1005Metric
- U2: footprint Package_SO:SOIC-8_5.23x5.23mm_P1.27mm -> Components:SOIC-8_5.23x5.23mm_P1.27mm
- U3: footprint RP2040_minimal:RP2040-QFN-56 -> Components:RP2040-QFN-56
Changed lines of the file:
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@@
 			)
 		)
-		(property "Footprint" "RP2040_minimal:RP2040-QFN-56"
+		(property "Footprint" "Components:RP2040-QFN-56"
 			(at 462.28 260.35 0)
 			(effects
@@
 			)
 		)
-		(property "Footprint" "Package_SO:SOIC-8_5.23x5.23mm_P1.27mm"
+		(property "Footprint" "Components:SOIC-8_5.23x5.23mm_P1.27mm"
 			(at 472.44 121.92 0)
 			(effects
@@
 			)
 		)
-		(property "Footprint" ""
+		(property "Footprint" "Resistor_SMD:R_0402_1005Metric"
 			(at 431.8 282.448 90)
 			(effects
@@
 		(on_board yes)
 		(dnp no)
-		(fields_autoplaced yes)
 		(property "Reference" "LED16"
 			(at 36.83 198.12 0)
@@
 			)
 		)
-		(property "Footprint" ""
+		(property "Footprint" "Components:USB-C_SMD-TYPE-C-31-M-12"
 			(at 510.54 88.9 0)
 			(effects
@@
 			)
 		)
-		(property "Footprint" ""
+		(property "Footprint" "Jumper:SolderJumper-2_P1.3mm_Open_TrianglePad1.0x1.5mm"
 			(at 422.91 285.75 0)
 			(effects
@@
 			)
 		)
-		(property "Footprint" ""
+		(property "Footprint" "Jumper:SolderJumper-2_P1.3mm_Open_TrianglePad1.0x1.5mm"
 			(at 414.02 119.38 0)
 			(effects
@@
 			)
 		)
-		(property "Footprint" ""
+		(property "Footprint" "Components:SSD1306-0.91-OLED-4pin-128x32"
 			(at 554.99 313.69 0)
 			(effects
@@
 			)
 		)
-		(property "Footprint" ""
+		(property "Footprint" "Resistor_SMD:R_0402_1005Metric"
 			(at 541.782 76.2 90)
 			(effects
@@
 			)
 		)
-		(property "Footprint" ""
+		(property "Footprint" "Resistor_SMD:R_0402_1005Metric"
 			(at 536.702 76.2 90)
 			(effects

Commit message: feat: start routing
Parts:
- removed SW1: SW_SPST, symbol Switch:SW_SPST
- added SW1: ON/OFF, Components:SW-SMD_XDMK-12C01-25, symbol XMDK-12C01-25:XDMK-12C01-25
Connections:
- net VBUS is gone; now on net VCC: C1.1, U1.3 (VI)
- net VCC: now also SW1.3
- net at J1.A4 (VBUS), J1.A9 (VBUS), J1.B4 (VBUS)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: now also SW1.2
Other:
- moved on the sheet: C1, C17

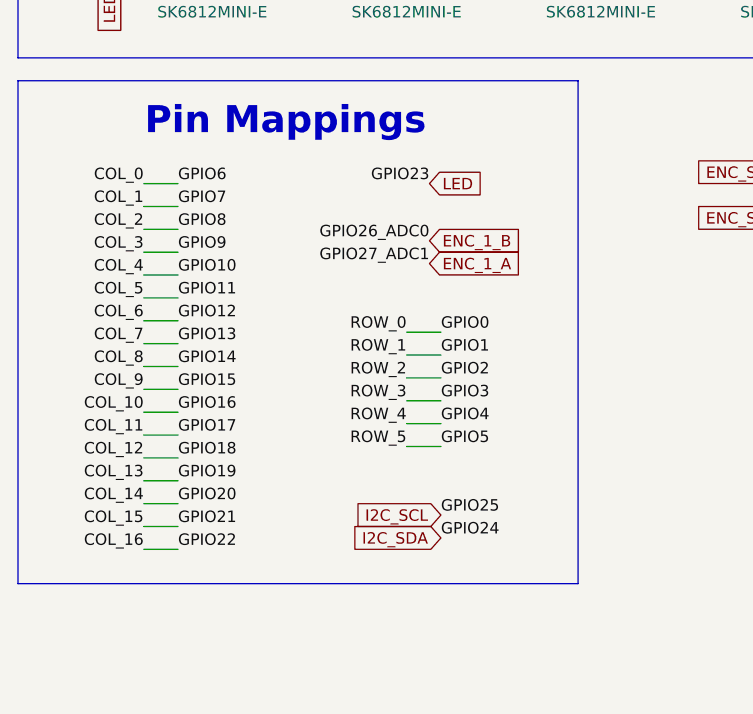
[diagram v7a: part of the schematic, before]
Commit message: feat: finish most of the routing
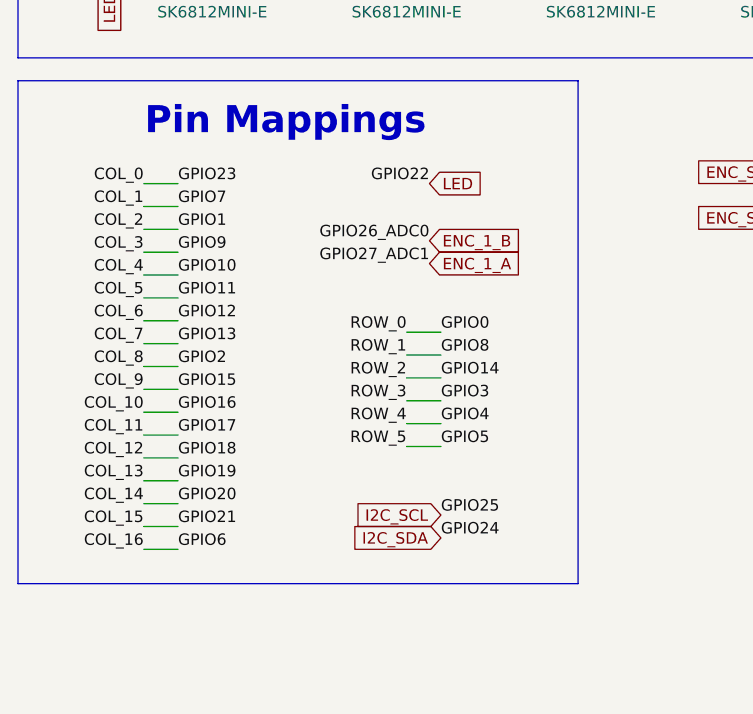
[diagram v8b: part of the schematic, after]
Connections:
- net COL_0: now also U3.35 (GPIO23); no longer U3.8 (GPIO6)
- net COL_16: now also U3.8 (GPIO6); no longer U3.34 (GPIO22)
- net COL_2: now also U3.3 (GPIO1); no longer U3.11 (GPIO8)
- net COL_8: now also U3.4 (GPIO2); no longer U3.17 (GPIO14)
- net LED: now also U3.34 (GPIO22); no longer U3.35 (GPIO23)
- net GPIO1 renamed GPIO8
- net GPIO8: now also U3.11 (GPIO8); no longer U3.3 (GPIO1)
- net GPIO2 renamed GPIO14
- net GPIO14: now also U3.17 (GPIO14); no longer U3.4 (GPIO2)
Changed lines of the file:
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@@
+		)
+	)
+	(label "GPIO2"
+		(at 33.02 360.68 0)
+		(effects
+			(font
+				(size 1.27 1.27)
+			)
+			(justify left bottom)
 		)
 	)
@@
 		)
 	)
-	(label "GPIO22"
-		(at 33.02 381 0)
-		(effects
-			(font
-				(size 1.27 1.27)
-			)
-			(justify left bottom)
-		)
-	)
 	(label "ROW_2"
 		(at 110.49 91.44 0)
@@
 		)
 	)
+	(label "GPIO23"
+		(at 33.02 340.36 0)
+		(effects
+			(font
+				(size 1.27 1.27)
+			)
+			(justify left bottom)
+		)
+	)
 	(label "GPIO25"
 		(at 528.32 290.83 180)
@@
 		)
 	)
-	(label "GPIO1"
-		(at 62.23 359.41 0)
-		(effects
-			(font
-				(size 1.27 1.27)
-			)
-			(justify left bottom)
-		)
-	)
 	(label "COL_11"
 		(at 252.73 71.12 180)
@@
 		)
 	)
-	(label "GPIO2"
-		(at 62.23 361.95 0)
-		(effects
-			(font
-				(size 1.27 1.27)
-			)
-			(justify left bottom)
-		)
-	)
 	(label "COL_7"
 		(at 171.45 71.12 180)
@@
 		)
 	)
+	(label "GPIO1"
+		(at 33.02 345.44 0)
+		(effects
+			(font
+				(size 1.27 1.27)
+			)
+			(justify left bottom)
+		)
+	)
 	(label "COL_14"
 		(at 359.41 52.07 180)
@@
 		)
 	)
+	(label "GPIO8"
+		(at 62.23 359.41 0)
+		(effects
+			(font
+				(size 1.27 1.27)
+			)
+			(justify left bottom)
+		)
+	)
 	(label "COL_1"
 		(at 74.93 109.22 180)
@@
 		)
 	)
+	(label "GPIO22"
+		(at 60.96 340.36 180)
+		(effects
+			(font
+				(size 1.27 1.27)
+			)
+			(justify right bottom)
+		)
+	)
 	(label "GPIO11"
 		(at 528.32 255.27 180)
@@
 		)
 	)
+	(label "GPIO14"
+		(at 62.23 361.95 0)
+		(effects
+			(font
+				(size 1.27 1.27)
+			)
+			(justify left bottom)
+		)
+	)
 	(label "COL_11"
 		(at 293.37 52.07 180)
@@
 		)
 	)
-	(label "GPIO8"
-		(at 33.02 345.44 0)
-		(effects
-			(font
-				(size 1.27 1.27)
-			)
-			(justify left bottom)
-		)
-	)
-	(label "GPIO6"
-		(at 33.02 340.36 0)
-		(effects
-			(font
-				(size 1.27 1.27)
-			)
-			(justify left bottom)
-		)
-	)
 	(label "ROW_4"
 		(at 146.05 116.84 0)
@@
 		)
 	)
-	(label "GPIO23"
-		(at 60.96 340.36 180)
-		(effects
-			(font
-				(size 1.27 1.27)
-			)
-			(justify right bottom)
-		)
-	)
 	(label "COL_15"
 		(at 29.21 378.46 180)
@@
 		)
 	)
+	(label "GPIO6"
+		(at 33.02 381 0)
+		(effects
+			(font
+				(size 1.27 1.27)
+			)
+			(justify left bottom)
+		)
+	)
 	(label "QSPI_SD2"
 		(at 445.77 124.46 0)
@@
 		(effects
 			(font
-				(size 1.27 1.27)
-			)
-			(justify left bottom)
-		)
-	)
-	(label "GPIO14"
-		(at 33.02 360.68 0)
-		(effects
-			(font
